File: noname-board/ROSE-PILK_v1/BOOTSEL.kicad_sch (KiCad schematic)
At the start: 3 parts, among them SW2 SW_Push_Dual

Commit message: Footprint Assignments
Assigned footprints to things that didn't currently have ones
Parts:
- R34, R35: footprint (none) -> Resistor_THT:R_Axial_DIN0207_L6.3mm_D2.5mm_P10.16mm_Horizontal
- SW2: footprint (none) -> Button_Switch_THT:SW_CuK_JS202011CQN_DPDT_Straight
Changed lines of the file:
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@@
       (effects (font (size 1.27 1.27)) (justify left))
     )
-    (property "Footprint" "" (at 121.412 58.42 90)
+    (property "Footprint" "Resistor_THT:R_Axial_DIN0207_L6.3mm_D2.5mm_P10.16mm_Horizontal" (at 121.412 58.42 90)
       (effects (font (size 1.27 1.27)) hide)
     )
@@
       (effects (font (size 1.27 1.27)) (justify left))
     )
-    (property "Footprint" "" (at 113.792 58.42 90)
+    (property "Footprint" "Resistor_THT:R_Axial_DIN0207_L6.3mm_D2.5mm_P10.16mm_Horizontal" (at 113.792 58.42 90)
       (effects (font (size 1.27 1.27)) hide)
     )
@@
       (effects (font (size 1.27 1.27)))
     )
-    (property "Footprint" "" (at 142.24 45.72 0)
+    (property "Footprint" "Button_Switch_THT:SW_CuK_JS202011CQN_DPDT_Straight" (at 142.24 45.72 0)
       (effects (font (size 1.27 1.27)) hide)
     )

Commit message: BootSel
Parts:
- removed R35: 1K, Resistor_THT:R_Axial_DIN0207_L6.3mm_D2.5mm_P10.16mm_Horizontal, symbol Device:R
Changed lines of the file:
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@@
   (junction (at 134.62 60.96) (diameter 0) (color 0 0 0 0)
-  )
-  (junction (at 123.19 67.31) (diameter 0) (color 0 0 0 0)
   )
   (wire (pts (xy 123.19 54.61) (xy 123.19 50.8))
@@
     (stroke (width 0) (type default))
   )
-  (wire (pts (xy 123.19 67.31) (xy 123.19 74.93))
-    (stroke (width 0) (type default))
-  )
-  (wire (pts (xy 115.57 49.53) (xy 115.57 54.61))
+  (wire (pts (xy 123.19 62.23) (xy 123.19 74.93))
     (stroke (width 0) (type default))
   )
@@
     (stroke (width 0) (type default))
   )
-  (wire (pts (xy 123.19 62.23) (xy 123.19 67.31))
-    (stroke (width 0) (type default))
-  )
-  (wire (pts (xy 115.57 67.31) (xy 123.19 67.31))
-    (stroke (width 0) (type default))
-  )
   (wire (pts (xy 147.32 50.8) (xy 152.4 50.8))
     (stroke (width 0) (type default))
@@
     (stroke (width 0) (type default))
   )
-  (wire (pts (xy 115.57 62.23) (xy 115.57 67.31))
-    (stroke (width 0) (type default))
-  )
   (hierarchical_label "QSPI_SS" (shape output) (at 123.19 74.93 270) (fields_autoplaced)
     (effects (font (size 1.27 1.27)) (justify right))
@@
   (hierarchical_label "GND" (shape input) (at 134.62 66.04 270) (fields_autoplaced)
     (effects (font (size 1.27 1.27)) (justify right))
-  )
-  (hierarchical_label "3v3" (shape input) (at 115.57 49.53 90) (fields_autoplaced)
-    (effects (font (size 1.27 1.27)) (justify left))
   )
   (symbol (lib_id "Device:R") (at 123.19 58.42 0) (unit 1)
@@
         )
       )
-    )
-  )
-  (symbol (lib_id "Device:R") (at 115.57 58.42 0) (unit 1)
-    (in_bom yes) (on_board yes) (dnp no) (fields_autoplaced)
-    (property "Reference" "R35" (at 118.11 57.15 0)
-      (effects (font (size 1.27 1.27)) (justify left))
-    )
-    (property "Value" "1K" (at 118.11 59.69 0)
-      (effects (font (size 1.27 1.27)) (justify left))
-    )
-    (property "Footprint" "Resistor_THT:R_Axial_DIN0207_L6.3mm_D2.5mm_P10.16mm_Horizontal" (at 113.792 58.42 90)
-      (effects (font (size 1.27 1.27)) hide)
-    )
-    (property "Datasheet" "~" (at 115.57 58.42 0)
-      (effects (font (size 1.27 1.27)) hide)
-    )
-    (pin "1")
-    (pin "2")
-    (instances
-      (project "ROSE-PILK_v1"
-        (path "/3dfb9737-68ba-4ca9-8085-72e4f57f9e50/0210b5e9-62f8-4096-ad3b-68b9f2dd9ed6"
-          (reference "R35") (unit 1)
-        )
-        (path "/3dfb9737-68ba-4ca9-8085-72e4f57f9e50/ee4b99aa-294b-4c3b-9b79-fbaf11f9a74b"
-          (reference "R36") (unit 1)
-        )
-      )

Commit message: Meeting Stuff
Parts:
- removed SW2: SW_Push_Dual, Button_Switch_THT:SW_CuK_JS202011CQN_DPDT_Straight, symbol Switch:SW_Push_Dual
- added S1: TL3301NF160QG, TL3301NF160QG:SW_TL3301NF160QG, symbol TL3301NF160QG:TL3301NF160QG
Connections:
- net GND: now also S1.2, S1.4
- net at R34.1: now also S1.1, S1.3
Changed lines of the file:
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@@
-    (stroke (width 0) (type default))
-  )
-  (wire (pts (xy 147.32 50.8) (xy 152.4 50.8))
     (stroke (width 0) (type default))
   )
   (wire (pts (xy 134.62 45.72) (xy 134.62 50.8))
-    (stroke (width 0) (type default))
-  )
-  (wire (pts (xy 147.32 55.88) (xy 152.4 55.88))
     (stroke (width 0) (type default))
   )
@@
     )
   )
-  (symbol (lib_id "Switch:SW_Push_Dual") (at 142.24 50.8 0) (unit 1)
-    (in_bom yes) (on_board yes) (dnp no)
-    (property "Reference" "SW2" (at 149.86 53.34 0)
+  (symbol (lib_id "TL3301NF160QG:TL3301NF160QG") (at 144.78 53.34 0) (unit 1)
+    (in_bom yes) (on_board yes) (dnp no) (fields_autoplaced)
+    (property "Reference" "S1" (at 144.78 44.45 0)
       (effects (font (size 1.27 1.27)))
     )
-    (property "Value" "SW_Push_Dual" (at 140.97 43.18 0)
+    (property "Value" "TL3301NF160QG" (at 144.78 46.99 0)
       (effects (font (size 1.27 1.27)))
     )
-    (property "Footprint" "Button_Switch_THT:SW_CuK_JS202011CQN_DPDT_Straight" (at 142.24 45.72 0)
+    (property "Footprint" "TL3301NF160QG:SW_TL3301NF160QG" (at 144.78 53.34 0)
+      (effects (font (size 1.27 1.27)) (justify bottom) hide)
+    )
+    (property "Datasheet" "" (at 144.78 53.34 0)
       (effects (font (size 1.27 1.27)) hide)
     )
-    (property "Datasheet" "~" (at 142.24 45.72 0)
-      (effects (font (size 1.27 1.27)) hide)
+    (property "MF" "E-Switch" (at 144.78 53.34 0)
+      (effects (font (size 1.27 1.27)) (justify bottom) hide)
+    )
+    (property "Purchase-URL" "https://www.snapeda.com/api/url_track_click_mouser/?unipart_id=304402&manufacturer=E-Switch&part_name=TL3301NF160QG&search_term=None" (at 144.78 53.34 0)
+      (effects (font (size 1.27 1.27)) (justify bottom) hide)
+    )
+    (property "Package" "None" (at 144.78 53.34 0)
+      (effects (font (size 1.27 1.27)) (justify bottom) hide)
+    )
+    (property "Price" "None" (at 144.78 53.34 0)
+      (effects (font (size 1.27 1.27)) (justify bottom) hide)
+    )
+    (property "Check_prices" "https://www.snapeda.com/parts/TL3301NF160QG/E-Switch/view-part/?ref=eda" (at 144.78 53.34 0)
+      (effects (font (size 1.27 1.27)) (justify bottom) hide)
+    )
+    (property "SnapEDA_Link" "https://www.snapeda.com/parts/TL3301NF160QG/E-Switch/view-part/?ref=snap" (at 144.78 53.34 0)
+      (effects (font (size 1.27 1.27)) (justify bottom) hide)
+    )
+    (property "MP" "TL3301NF160QG" (at 144.78 53.34 0)
+      (effects (font (size 1.27 1.27)) (justify bottom) hide)
+    )
+    (property "Availability" "In Stock" (at 144.78 53.34 0)
+      (effects (font (size 1.27 1.27)) (justify bottom) hide)
+    )
+    (property "Description" "\nTactile Switch, TL3301, SPST-NO, OFF-(ON), 4.3mm Top Actuated, 0.05A, 12VDC | E-Switch TL3301NF160QG\n" (at 144.78 53.34 0)
+      (effects (font (size 1.27 1.27)) (justify bottom) hide)
     )
     (pin "1")
@@
     (instances
       (project "ROSE-PILK_v1"
-        (path "/3dfb9737-68ba-4ca9-8085-72e4f57f9e50/0210b5e9-62f8-4096-ad3b-68b9f2dd9ed6"
-          (reference "SW2") (unit 1)
-        )
         (path "/3dfb9737-68ba-4ca9-8085-72e4f57f9e50/ee4b99aa-294b-4c3b-9b79-fbaf11f9a74b"
-          (reference "SW3") (unit 1)
+          (reference "S1") (unit 1)
         )
       )

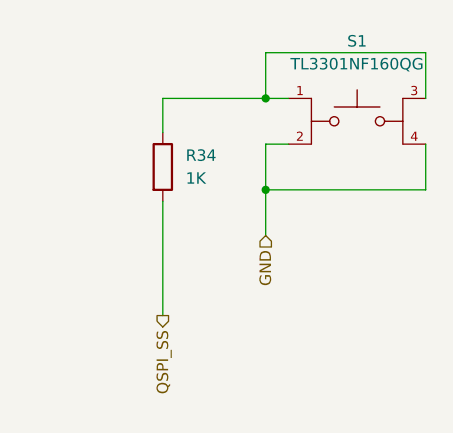
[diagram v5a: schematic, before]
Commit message: Document-Updated Version
Used the Pico Doc to update the Power, Flash, and BootSel schematics.
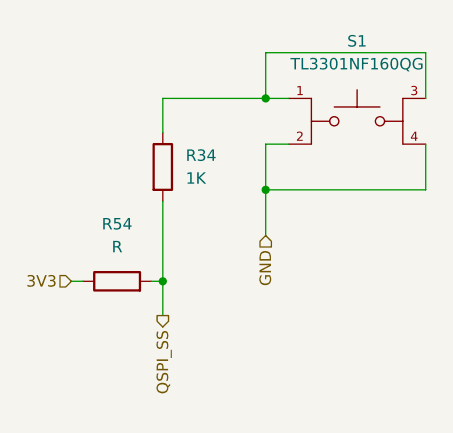
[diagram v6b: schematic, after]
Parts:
- added R54: R, Resistor_THT:R_Axial_DIN0207_L6.3mm_D2.5mm_P10.16mm_Horizontal, symbol Device:R
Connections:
- net QSPI_SS: now also R54.2
- new net 3V3: R54.1
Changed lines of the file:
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@@
   (junction (at 134.62 60.96) (diameter 0) (color 0 0 0 0)
   )
+  (junction (at 123.19 71.12) (diameter 0) (color 0 0 0 0)
+  )
   (wire (pts (xy 123.19 54.61) (xy 123.19 50.8))
+    (stroke (width 0) (type default))
+  )
+  (wire (pts (xy 121.92 71.12) (xy 123.19 71.12))
     (stroke (width 0) (type default))
   )
@@
     (stroke (width 0) (type default))
   )
-  (wire (pts (xy 123.19 62.23) (xy 123.19 74.93))
+  (wire (pts (xy 123.19 62.23) (xy 123.19 71.12))
+    (stroke (width 0) (type default))
+  )
+  (wire (pts (xy 123.19 71.12) (xy 123.19 74.93))
     (stroke (width 0) (type default))
   )
@@
     (stroke (width 0) (type default))
   )
+  (wire (pts (xy 113.03 71.12) (xy 114.3 71.12))
+    (stroke (width 0) (type default))
+  )
   (wire (pts (xy 134.62 45.72) (xy 134.62 50.8))
     (stroke (width 0) (type default))
@@
   )
   (hierarchical_label "GND" (shape input) (at 134.62 66.04 270) (fields_autoplaced)
+    (effects (font (size 1.27 1.27)) (justify right))
+  )
+  (hierarchical_label "3V3" (shape input) (at 113.03 71.12 180) (fields_autoplaced)
     (effects (font (size 1.27 1.27)) (justify right))
   )
@@
         )
       )
+    )
+  )
+  (symbol (lib_id "Device:R") (at 118.11 71.12 90) (unit 1)
+    (in_bom yes) (on_board yes) (dnp no) (fields_autoplaced)
+    (property "Reference" "R54" (at 118.11 64.77 90)
+      (effects (font (size 1.27 1.27)))
+    )
+    (property "Value" "R" (at 118.11 67.31 90)
+      (effects (font (size 1.27 1.27)))
+    )
+    (property "Footprint" "Resistor_THT:R_Axial_DIN0207_L6.3mm_D2.5mm_P10.16mm_Horizontal" (at 118.11 72.898 90)
+      (effects (font (size 1.27 1.27)) hide)
+    )
+    (property "Datasheet" "~" (at 118.11 71.12 0)
+      (effects (font (size 1.27 1.27)) hide)
+    )
+    (pin "1")
+    (pin "2")
+    (instances
+      (project "ROSE-PILK_v1"
+        (path "/3dfb9737-68ba-4ca9-8085-72e4f57f9e50/ee4b99aa-294b-4c3b-9b79-fbaf11f9a74b"
+          (reference "R54") (unit 1)
+        )
+        (path "/3dfb9737-68ba-4ca9-8085-72e4f57f9e50/853a186f-a31e-46ca-9745-e888a8f62939"
+          (reference "R55") (unit 1)
+        )
+      )

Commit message: Ben
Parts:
- removed R54: R, Resistor_THT:R_Axial_DIN0207_L6.3mm_D2.5mm_P10.16mm_Horizontal, symbol Device:R
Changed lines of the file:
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@@
   (junction (at 134.62 60.96) (diameter 0) (color 0 0 0 0)
   )
-  (junction (at 123.19 71.12) (diameter 0) (color 0 0 0 0)
-  )
   (wire (pts (xy 123.19 54.61) (xy 123.19 50.8))
-    (stroke (width 0) (type default))
-  )
-  (wire (pts (xy 121.92 71.12) (xy 123.19 71.12))
     (stroke (width 0) (type default))
   )
@@
     (stroke (width 0) (type default))
   )
-  (wire (pts (xy 123.19 62.23) (xy 123.19 71.12))
-    (stroke (width 0) (type default))
-  )
-  (wire (pts (xy 123.19 71.12) (xy 123.19 74.93))
+  (wire (pts (xy 123.19 62.23) (xy 123.19 74.93))
     (stroke (width 0) (type default))
   )
@@
     (stroke (width 0) (type default))
   )
-  (wire (pts (xy 113.03 71.12) (xy 114.3 71.12))
-    (stroke (width 0) (type default))
-  )
   (wire (pts (xy 134.62 45.72) (xy 134.62 50.8))
     (stroke (width 0) (type default))
@@
   )
   (hierarchical_label "GND" (shape input) (at 134.62 66.04 270) (fields_autoplaced)
-    (effects (font (size 1.27 1.27)) (justify right))
-  )
-  (hierarchical_label "3V3" (shape input) (at 113.03 71.12 180) (fields_autoplaced)
     (effects (font (size 1.27 1.27)) (justify right))
   )
@@
         )
       )
-    )
-  )
-  (symbol (lib_id "Device:R") (at 118.11 71.12 90) (unit 1)
-    (in_bom yes) (on_board yes) (dnp no) (fields_autoplaced)
-    (property "Reference" "R54" (at 118.11 64.77 90)
-      (effects (font (size 1.27 1.27)))
-    )
-    (property "Value" "R" (at 118.11 67.31 90)
-      (effects (font (size 1.27 1.27)))
-    )
-    (property "Footprint" "Resistor_THT:R_Axial_DIN0207_L6.3mm_D2.5mm_P10.16mm_Horizontal" (at 118.11 72.898 90)
-      (effects (font (size 1.27 1.27)) hide)
-    )
-    (property "Datasheet" "~" (at 118.11 71.12 0)
-      (effects (font (size 1.27 1.27)) hide)
-    )
-    (pin "1")
-    (pin "2")
-    (instances
-      (project "ROSE-PILK_v1"
-        (path "/3dfb9737-68ba-4ca9-8085-72e4f57f9e50/ee4b99aa-294b-4c3b-9b79-fbaf11f9a74b"
-          (reference "R54") (unit 1)
-        )
-        (path "/3dfb9737-68ba-4ca9-8085-72e4f57f9e50/853a186f-a31e-46ca-9745-e888a8f62939"
-          (reference "R55") (unit 1)
-        )
-      )
